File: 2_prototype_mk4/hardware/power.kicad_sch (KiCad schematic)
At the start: 2 parts, among them J2 Conn_01x04_Pin

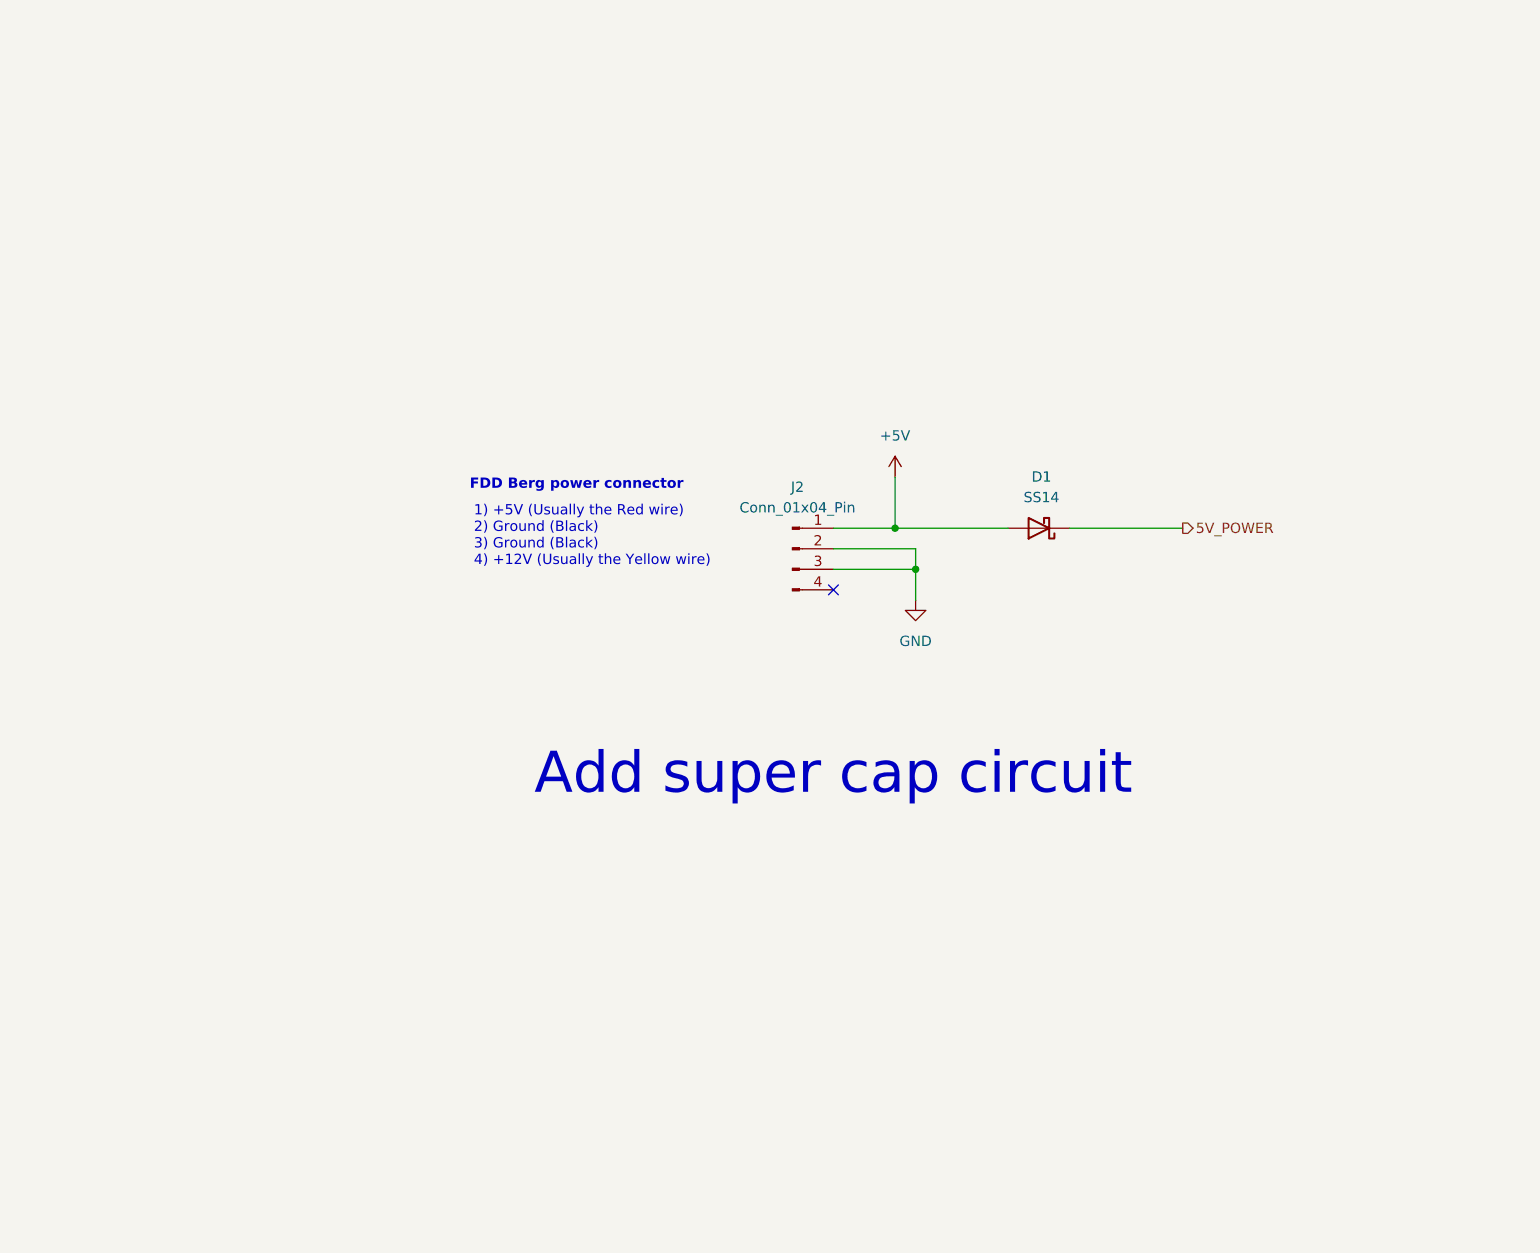
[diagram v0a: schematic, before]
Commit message: Create initial MK4 PCB layout
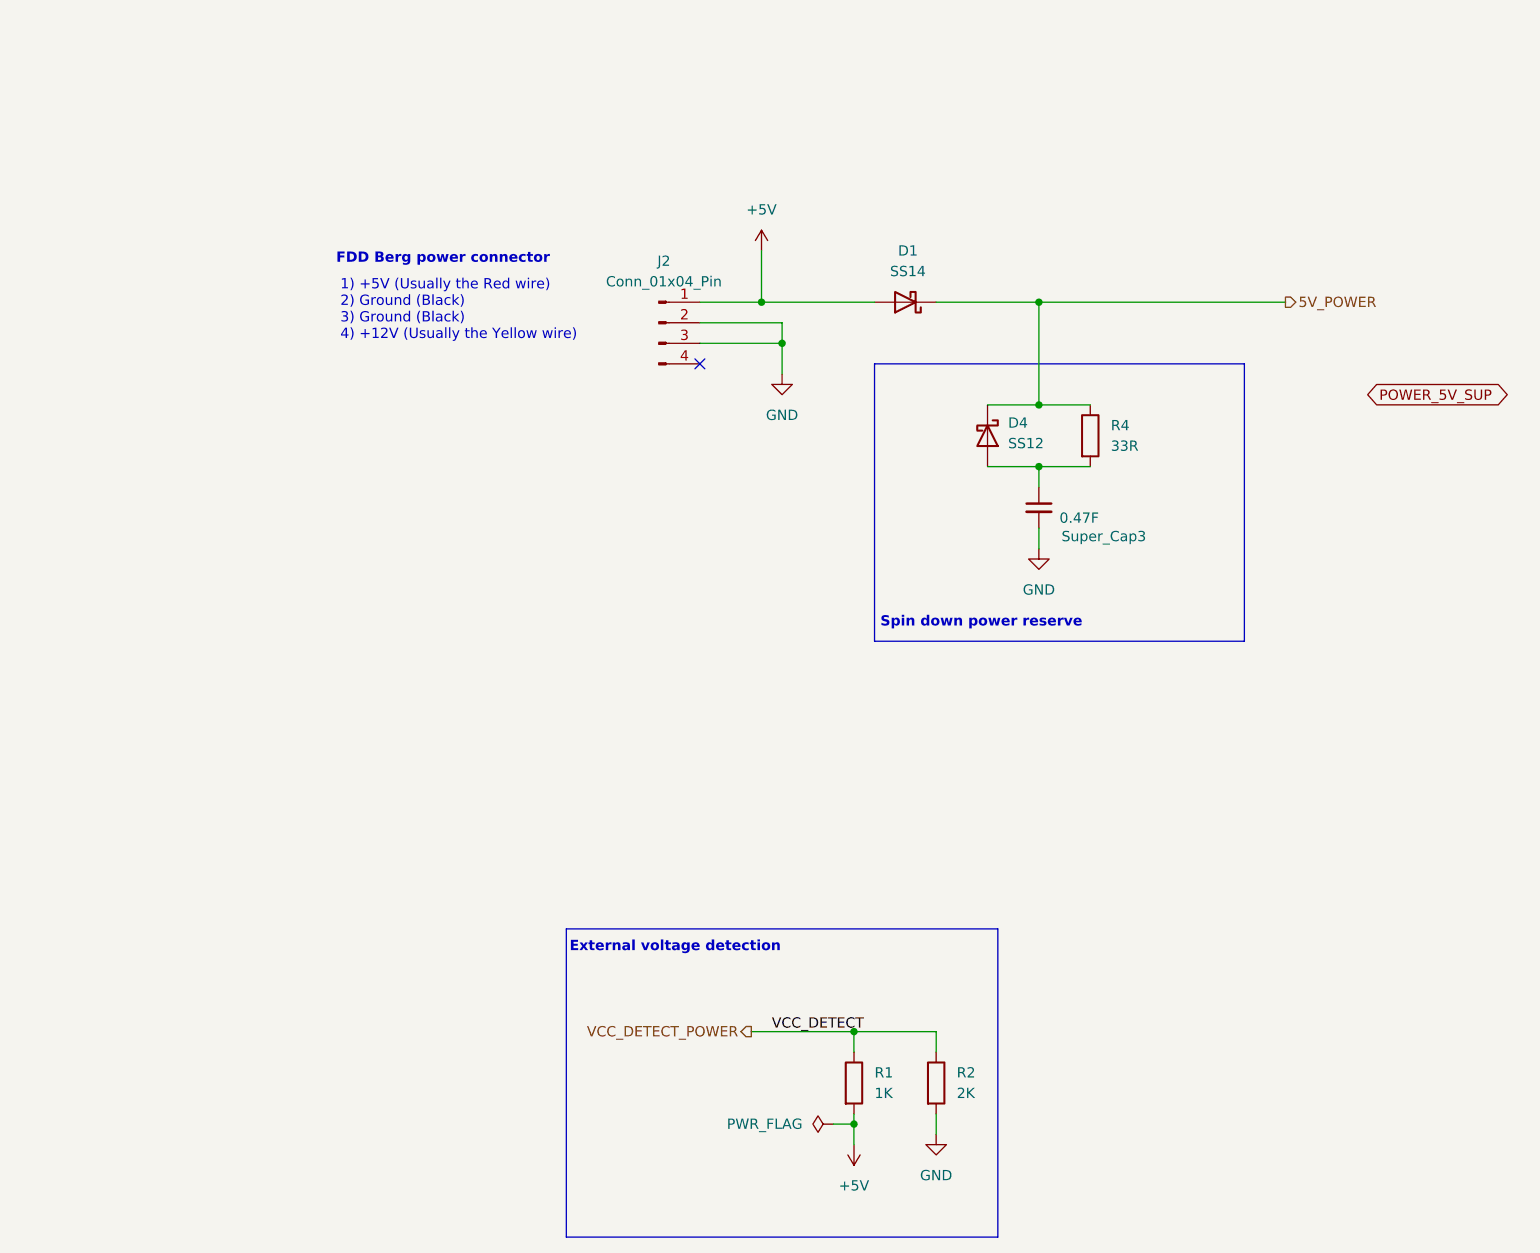
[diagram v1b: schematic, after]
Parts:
- added D4: SS12, Diode_SMD:D_SMA, symbol Device:D_Schottky
- added R1: 1K, Resistor_SMD:R_0603_1608Metric, symbol Device:R
- added R2: 2K, Resistor_SMD:R_0603_1608Metric, symbol Device:R
- added R4: 33R, Resistor_SMD:R_1206_3216Metric, symbol Device:R
- added Super_Cap3: 0.47F, Capacitor_THT:CP_Radial_D12.5mm_P5.00mm, symbol Device:C_Small
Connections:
- net +5V: now also R1.2
- net 5V_POWER: now also D4.1 (K), R4.1
- net GND: now also R2.2, Super_Cap3.2
- new net: D4.2 (A), R4.2, Super_Cap3.1
- new net VCC_DETECT_POWER: R1.1, R2.1
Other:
- note added: "External voltage detection"
- note added: "Spin down power reserve"
- note removed: "Add super cap circuit"
- moved on the sheet: D1, J2

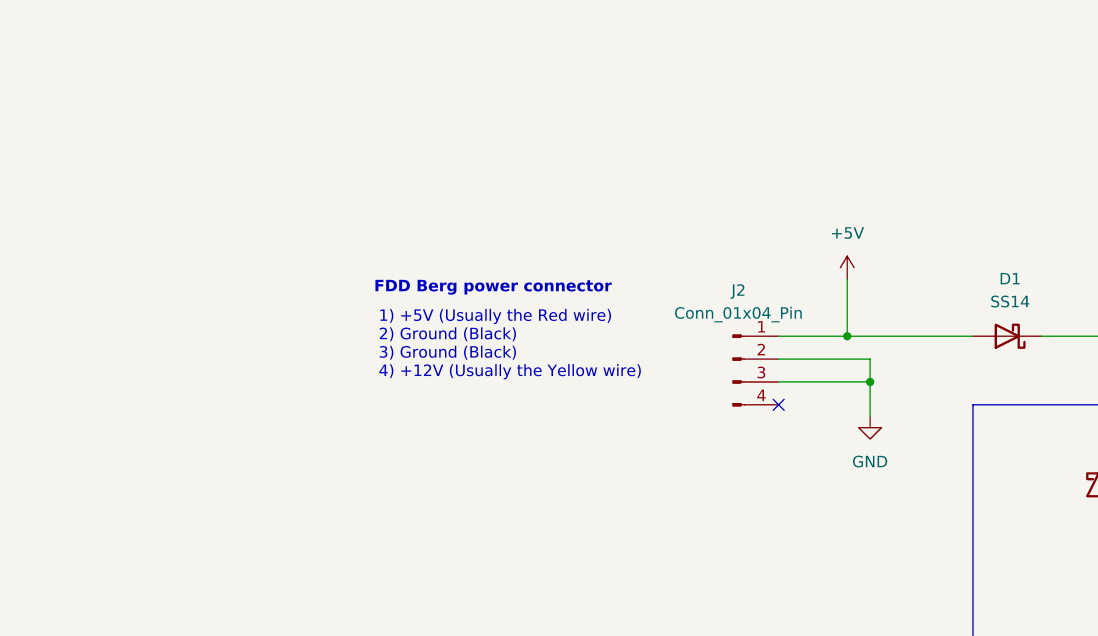
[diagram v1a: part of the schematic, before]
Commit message: Placed all components on PCB
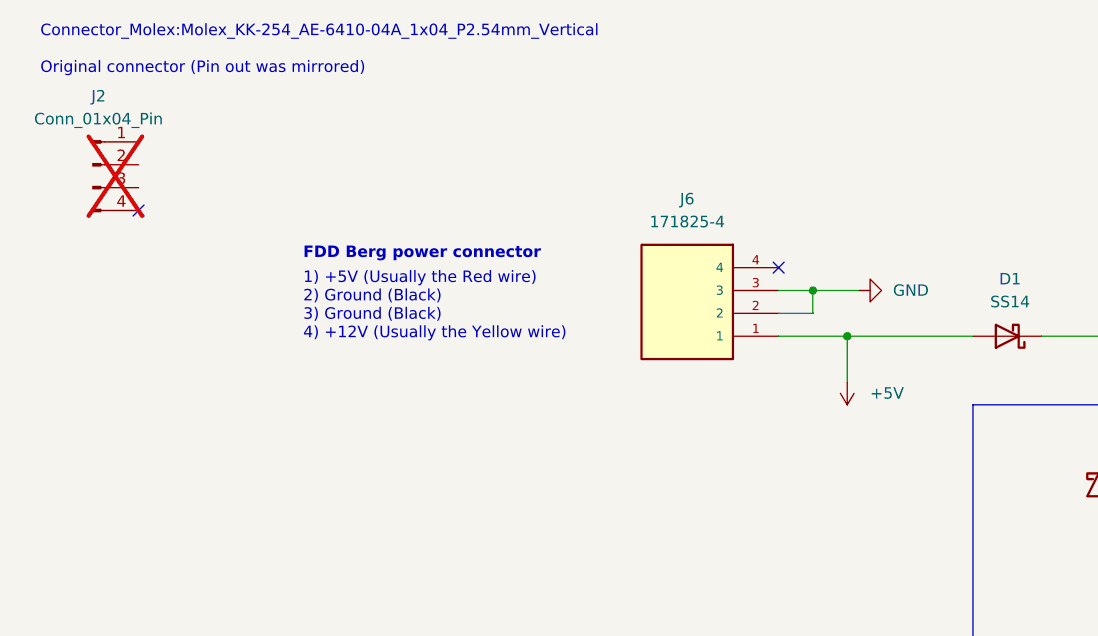
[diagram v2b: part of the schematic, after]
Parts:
- added J6: 171825-4, Custom:TE_171825-4, symbol Project symbols:171825-4
- J2: now not fitted; now left out of the parts list
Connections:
- net +5V: now also J6.1; no longer J2.1 (Pin_1)
- net GND: now also J6.2, J6.3; no longer J2.2 (Pin_2), J2.3 (Pin_3)
- no-connect marks 1 -> 2
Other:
- note added: "Connector_Molex:Molex_KK-254_AE-6410-04A_1x04_P2.54mm_Vertical Original connector (Pin out was mirrored)"
